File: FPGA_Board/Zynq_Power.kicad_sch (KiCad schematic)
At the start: 0 parts

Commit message: add FPGA,DDR, Decoupling capacitor symbols for power & ddr sheets. modify symbols pinout placement to clean up schematic
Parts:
- added C10, C11, C5, C6, C7, C8, C9: C, symbol Device:C
- added U5: XC7Z010-2CLG400I, FPGA_BOARD:CLG400, symbol FPGA_Parts:CMP-0363-00008-3
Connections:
- new net +1V0: C7.1, C8.1, U5.G13 (VCCINT), U5.G7 (VCCPINT), U5.H12 (VCCINT), U5.J13 (VCCINT), U5.J7 (VCCPINT), U5.K12 (VCCINT), U5.L13 (VCCINT), U5.L7 (VCCPINT), U5.M12 (VCCINT), U5.N13 (VCCINT), U5.N7 (VCCPINT), U5.P12 (VCCINT), U5.P8 (VCCPINT), U5.R13 (VCCINT), U5.R7 (VCCPINT)
- new net +1V8: C5.1, U5.A13 (VCCO_MIO1_501), U5.B16 (VCCO_MIO1_501), U5.D12 (VCCO_MIO1_501), U5.E15 (VCCO_MIO1_501)
- new net +3V3: C10.1, C11.1, C6.1, C9.1, U5.B6 (VCCO_MIO0_500), U5.C19 (VCCO_35), U5.D7 (VCCO_MIO0_500), U5.F18 (VCCO_35), U5.H14 (VCCO_35), U5.J17 (VCCO_35), U5.K20 (VCCO_35), U5.K6 (VCCO_0), U5.M16 (VCCO_35), U5.N19 (VCCO_34), U5.N6 (RSVDVCC3), U5.R15 (VCCO_34), U5.R6 (RSVDVCC2), U5.T18 (VCCO_34), U5.T6 (RSVDVCC1), U5.T8 (VCCO_13), U5.U11 (VCCO_13), U5.V14 (VCCO_34), U5.W17 (VCCO_34), U5.W7 (VCCO_13), U5.Y10 (VCCO_13), U5.Y20 (VCCO_34)
- new net GND: C10.2, C11.2, C5.2, C6.2, C7.2, C8.2, C9.2

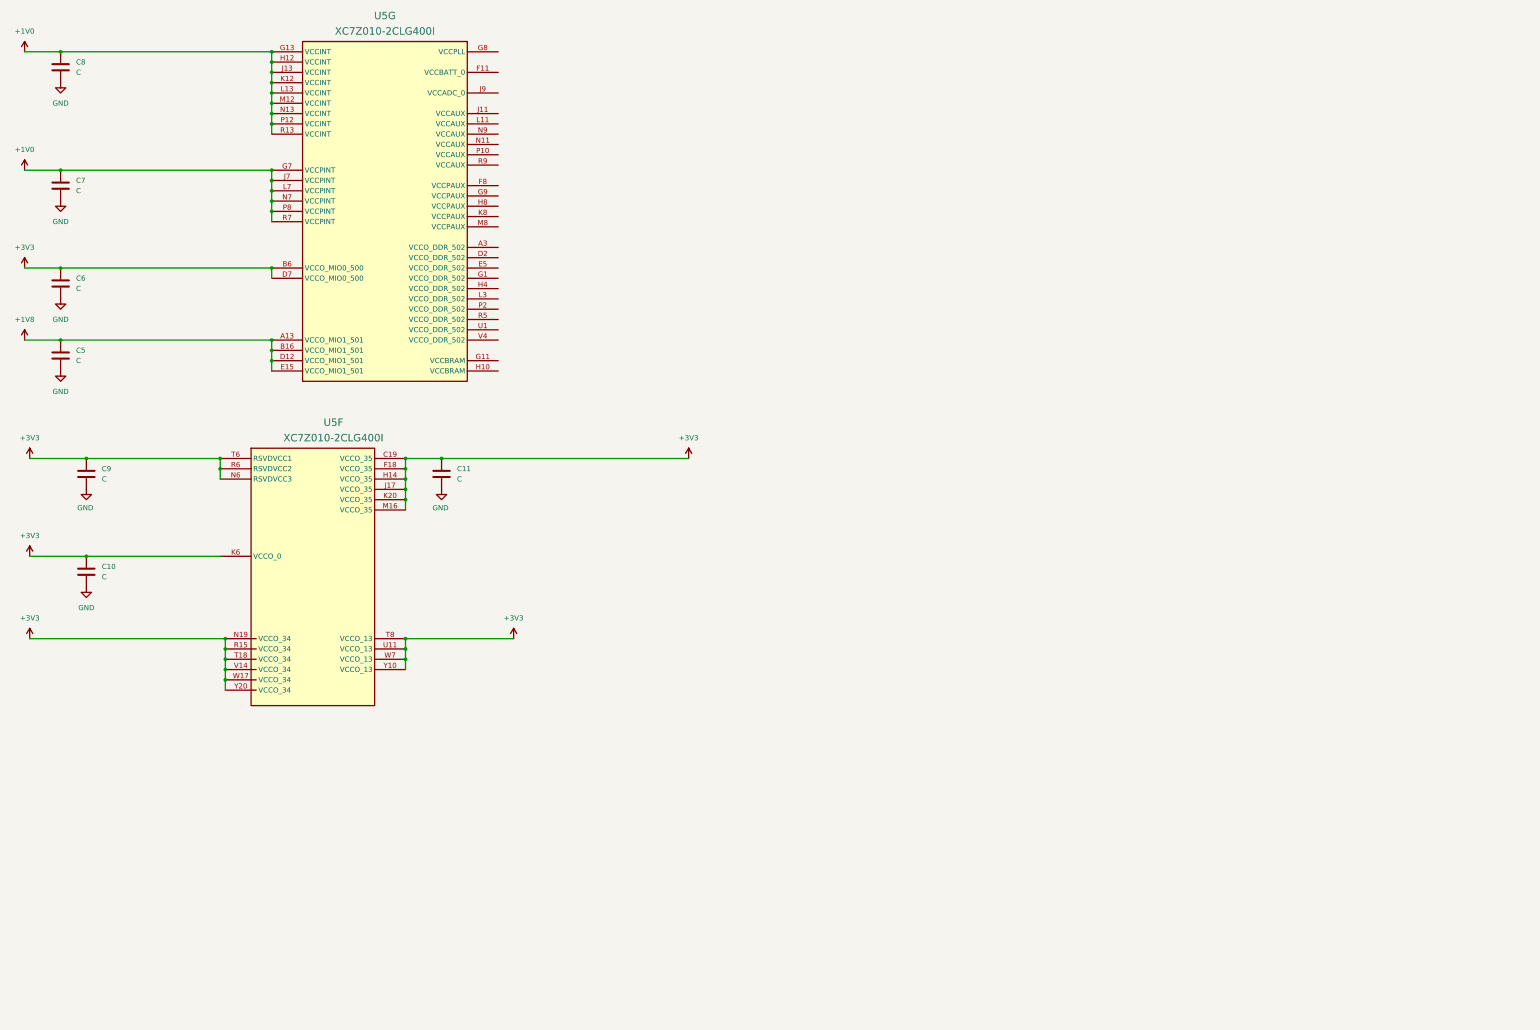
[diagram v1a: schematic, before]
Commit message: Add DDR VTT power module, add Zynq power + decoupling, placed Zynq DDR
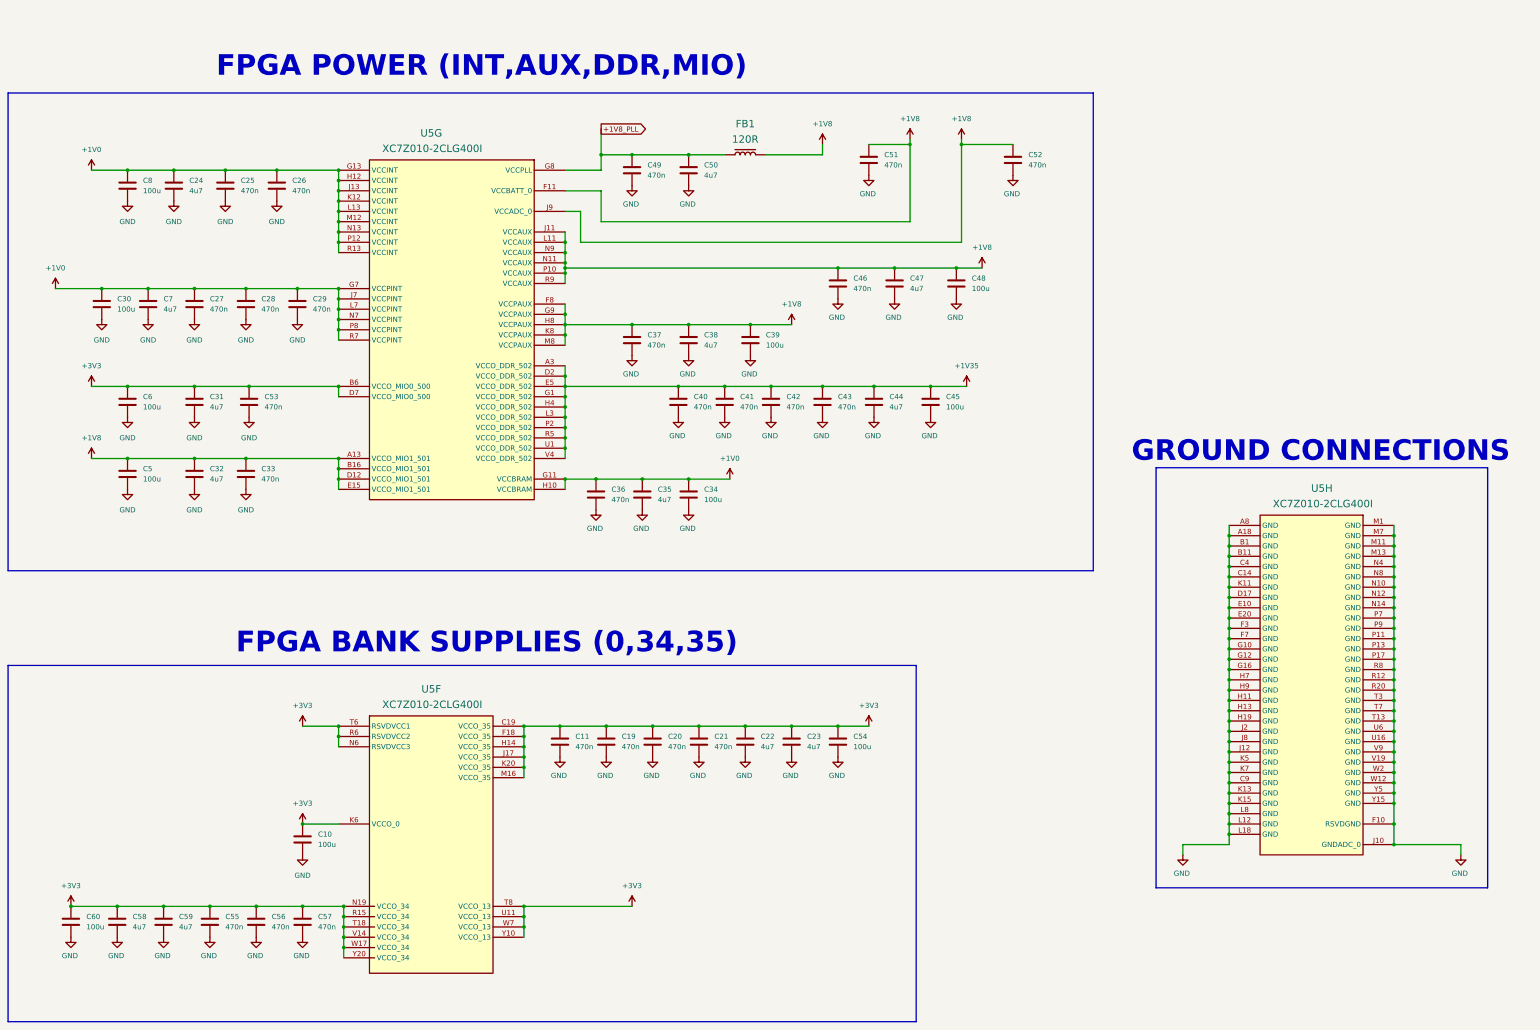
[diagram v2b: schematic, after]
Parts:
- removed C9: C, symbol Device:C
- added C19, C20, C21, C25, C26, C27, C28, C29, C33, C36, C37, C40, C41, C42, C43, C46, C49, C51, C52, C53, C55, C56, C57: 470n, symbol Device:C
- added C22, C23, C24, C31, C32, C35, C38, C44, C47, C50, C58, C59: 4u7, symbol Device:C
- added C30, C34, C39, C45, C48, C54, C60: 100u, symbol Device:C
- added FB1: 120R, FPGA_BOARD:FB_0402, symbol FPGA_Parts:FB_0402
- added unit 6 of U5
- C10, C5, C6, C8: value C -> 100u
- C11: value C -> 470n
- C7: value C -> 4u7
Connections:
- net +1V0: now also U5.G11 (VCCBRAM), U5.H10 (VCCBRAM), C24.1, C25.1, C26.1, C27.1, C28.1, C29.1, C30.1, C34.1, C35.1, C36.1
- net +1V8: now also U5.F11 (VCCBATT_0), U5.F8 (VCCPAUX), U5.G9 (VCCPAUX), U5.H8 (VCCPAUX), U5.J11 (VCCAUX), U5.J9 (VCCADC_0), U5.K8 (VCCPAUX), U5.L11 (VCCAUX), U5.M8 (VCCPAUX), U5.N11 (VCCAUX), U5.N9 (VCCAUX), U5.P10 (VCCAUX), U5.R9 (VCCAUX), C32.1, C33.1, C37.1, C38.1, C39.1, C46.1, C47.2, C48.1, C51.1, C52.1, FB1.2
- net +3V3: now also C19.1, C20.1, C21.1, C22.1, C23.1, C31.1, C53.1, C54.1, C55.1, C56.1, C57.1, C58.1, C59.1, C60.1, U5.C19 (VCCO_35), U5.F18 (VCCO_35), U5.H14 (VCCO_35), U5.J17 (VCCO_35), U5.K20 (VCCO_35), U5.K6 (VCCO_0), U5.M16 (VCCO_35), U5.N19 (VCCO_34), U5.N6 (RSVDVCC3), U5.R15 (VCCO_34), U5.R6 (RSVDVCC2), U5.T18 (VCCO_34), U5.T6 (RSVDVCC1), U5.T8 (VCCO_13), U5.U11 (VCCO_13), U5.V14 (VCCO_34), U5.W17 (VCCO_34), U5.W7 (VCCO_13), U5.Y10 (VCCO_13), U5.Y20 (VCCO_34); no longer U5.C19 (VCCO_35), U5.F18 (VCCO_35), U5.H14 (VCCO_35), U5.J17 (VCCO_35), U5.K20 (VCCO_35), U5.K6 (VCCO_0), U5.M16 (VCCO_35), U5.N19 (VCCO_34), U5.N6 (RSVDVCC3), U5.R15 (VCCO_34), U5.R6 (RSVDVCC2), U5.T18 (VCCO_34), U5.T6 (RSVDVCC1), U5.T8 (VCCO_13), U5.U11 (VCCO_13), U5.V14 (VCCO_34), U5.W17 (VCCO_34), U5.W7 (VCCO_13), U5.Y10 (VCCO_13), U5.Y20 (VCCO_34)
- net GND: now also C19.2, C20.2, C21.2, C22.2, C23.2, C24.2, C25.2, C26.2, C27.2, C28.2, C29.2, C30.2, C31.2, C32.2, C33.2, C34.2, C35.2, C36.2, C37.2, C38.2, C39.2, C40.2, C41.2, C42.2, C43.2, C44.2, C45.2, C46.2, C47.1, C48.2, C49.2, C50.2, C51.2, C52.2, C53.2, C54.2, C55.2, C56.2, C57.2, C58.2, C59.2, C60.2, U5.A18 (GND), U5.A8 (GND), U5.B1 (GND), U5.B11 (GND), U5.C14 (GND), U5.C4 (GND), U5.C9 (GND), U5.D17 (GND), U5.E10 (GND), U5.E20 (GND), U5.F10 (RSVDGND), U5.F3 (GND), U5.F7 (GND), U5.G10 (GND), U5.G12 (GND), U5.G16 (GND), U5.H11 (GND), U5.H13 (GND), U5.H19 (GND), U5.H7 (GND), U5.H9 (GND), U5.J10 (GNDADC_0), U5.J12 (GND), U5.J2 (GND), U5.J8 (GND), U5.K11 (GND), U5.K13 (GND), U5.K15 (GND), U5.K5 (GND), U5.K7 (GND), U5.L12 (GND), U5.L18 (GND), U5.L8 (GND), U5.M1 (GND), U5.M11 (GND), U5.M13 (GND), U5.M7 (GND), U5.N10 (GND), U5.N12 (GND), U5.N14 (GND), U5.N4 (GND), U5.N8 (GND), U5.P11 (GND), U5.P13 (GND), U5.P17 (GND), U5.P7 (GND), U5.P9 (GND), U5.R12 (GND), U5.R20 (GND), U5.R8 (GND), U5.T13 (GND), U5.T3 (GND), U5.T7 (GND), U5.U16 (GND), U5.U6 (GND), U5.V19 (GND), U5.V9 (GND), U5.W12 (GND), U5.W2 (GND), U5.Y15 (GND), U5.Y5 (GND)
- net +1V35: now reaches U5.A3 (VCCO_DDR_502)
- net +1V35: now also U5.D2 (VCCO_DDR_502), U5.E5 (VCCO_DDR_502), U5.G1 (VCCO_DDR_502), U5.H4 (VCCO_DDR_502), U5.L3 (VCCO_DDR_502), U5.P2 (VCCO_DDR_502), U5.R5 (VCCO_DDR_502), U5.U1 (VCCO_DDR_502), U5.V4 (VCCO_DDR_502), C40.1, C41.1, C42.1, C43.1, C44.1, C45.1
- net +1V8_PLL: now reaches U5.G8 (VCCPLL)
- net +1V8_PLL: now also C49.1, C50.1, FB1.1
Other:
- note added: "FPGA BANK SUPPLIES (0,34,35)"
- note added: "FPGA POWER (INT,AUX,DDR,MIO)"
- note added: "GROUND CONNECTIONS"
- moved on the sheet: C10, C11, C5, C6, C7, C8, U5G
